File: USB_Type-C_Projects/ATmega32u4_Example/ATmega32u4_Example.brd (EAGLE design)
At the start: 29.1 x 61.5 mm, 8 parts, among them J2 105450-0101, U1 ATMEGA32U4-AU, U2 IP4234CZ6,125

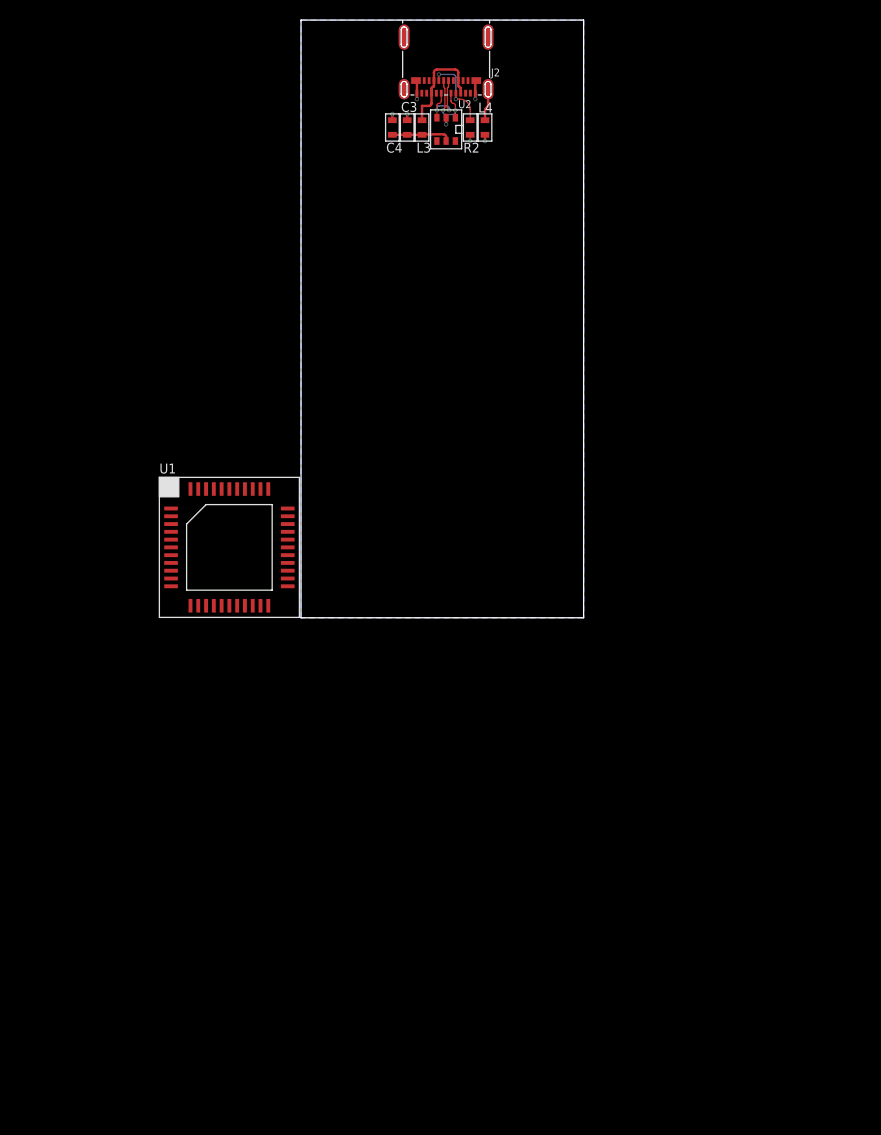
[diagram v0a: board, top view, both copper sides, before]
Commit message: USB connections made.
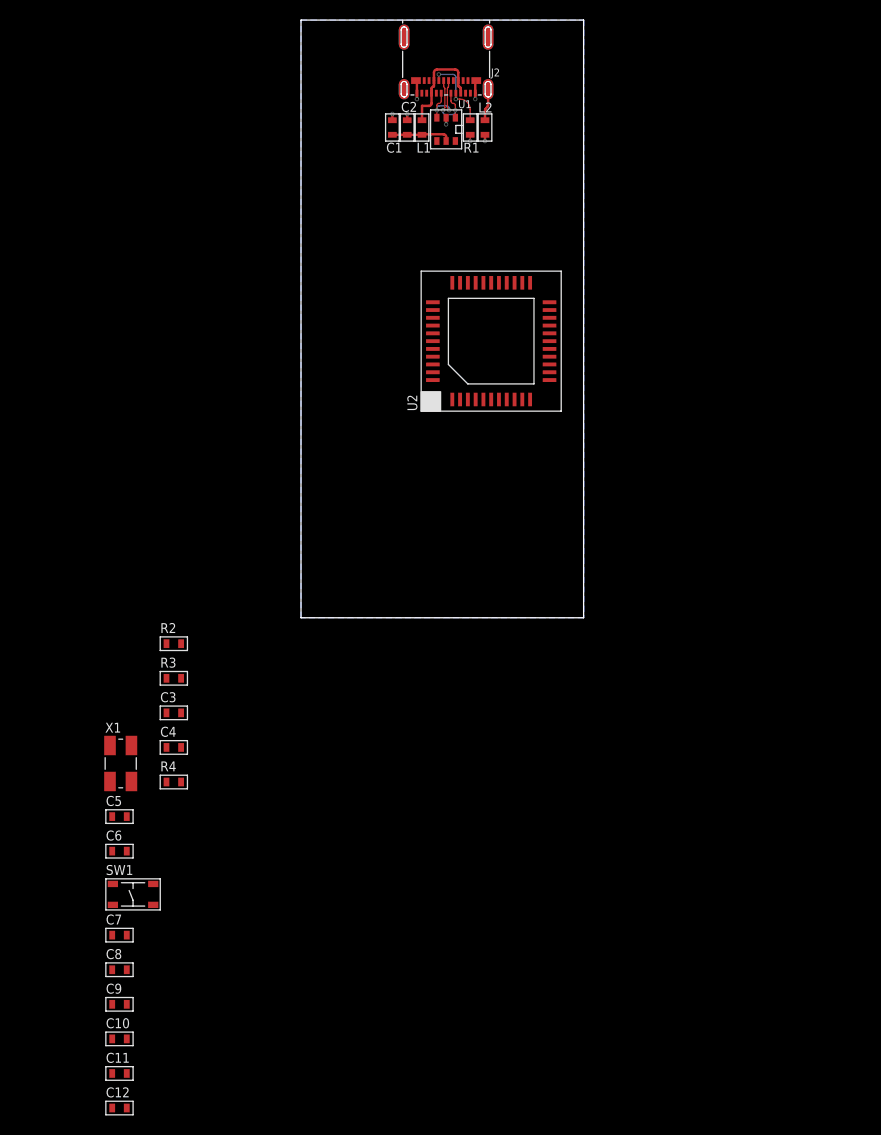
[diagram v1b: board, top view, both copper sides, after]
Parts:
- added C1: 1uF, MF_Passives:C0603
- added C10, C11, C12, C2, C7, C8, C9: 0.1uF, MF_Passives:C0603
- added C5, C6: 22pF, MF_Passives:C0603
- added R1: 5.1K, MF_Passives:R0603
- added R3: 22, MF_Passives:R0603
- added R4: 10K, MF_Passives:R0603
- added SW1: MF-SW-TACT-4.2MM, MF_Switches:TACT4.2MM
- added X1: ABM3B-16.000MHZ-D-1-X-T, MF_Frequency_Control:5MMX3.2MM
- C3: value 0.1uF -> 1uF
- C4: value 1uF -> 0.1uF
- R2: value 5.1K -> 22
- U1: value ATMEGA32U4-AU -> IP4234CZ6,125; device MF_IC_Digital:TQFP44 -> PP_Passives:IP4234CZ6_SOT-457-6
- U2: value IP4234CZ6,125 -> ATMEGA32U4-AU; device PP_Passives:IP4234CZ6_SOT-457-6 -> MF_IC_Digital:TQFP44
- moved C4 67.6 mm to (-13.1, -13.3), turned to 0 degrees
- moved C3 64.8 mm to (-13.1, -9.78), turned to 0 degrees
- moved R2 61.2 mm to (-13.1, -2.67), turned to 0 degrees
- moved U1 48.4 mm to (14.9, 50.2), turned to 270 degrees
- moved U2 22.3 mm to (19.6, 28.4), turned to 90 degrees
- renumbered L3 to L1, L4 to L2
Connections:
- removed net AREF: U1.P$42
- removed net AVCC: U1.P$24, U1.P$44
- removed net UCAP: U1.P$6
- removed net UGND: U1.P$5
- removed net UVCC: U1.P$2
- removed net VBUS: U1.P$7
- removed net VCC: U1.P$14, U1.P$34
- new net N$1: R2.P$2, U2.P$3
- new net N$2: R3.P$2, U2.P$4
- new net N$3: C3.P$2, U2.P$6
- new net N$4: C4.P$2, U2.P$42
- new net RESET: R4.P$2, SW1.P$1, SW1.P$2, U2.P$13
- new net XTAL1: C5.P$1, U2.P$17, X1.P$1
- new net XTAL2: C6.P$1, U2.P$16, X1.P$3
- net CC1/1: now also R1.P$1; no longer R2.P$1
- net D+: now also U1.1; no longer U2.1
- net D-: now also U1.3; no longer U2.3
- net DM: now also R2.P$1, U1.4; no longer U2.4
- net DP: now also R3.P$1, U1.6; no longer U2.6
- net GND: now also C1.P$2, C10.P$2, C11.P$2, C12.P$2, C2.P$2, C3.P$1, C4.P$1, C5.P$2, C6.P$2, C7.P$2, C8.P$2, C9.P$2, R1.P$2, SW1.P$3, SW1.P$4, U1.2, U2.P$15, U2.P$23, U2.P$35, U2.P$43, U2.P$5, X1.P$2, X1.P$4; no longer C3.P$2, C4.P$2, R2.P$2, U1.P$15, U1.P$23, U1.P$35, U1.P$43, U2.2
- net USB_VBUS: now also C1.P$1, C10.P$1, C11.P$1, C12.P$1, C2.P$1, C7.P$1, C8.P$1, C9.P$1, R4.P$1, U1.5, U2.P$14, U2.P$2, U2.P$24, U2.P$34, U2.P$44, U2.P$7; no longer C3.P$1, C4.P$1, U2.5

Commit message: Schematic complete. Parts placed.
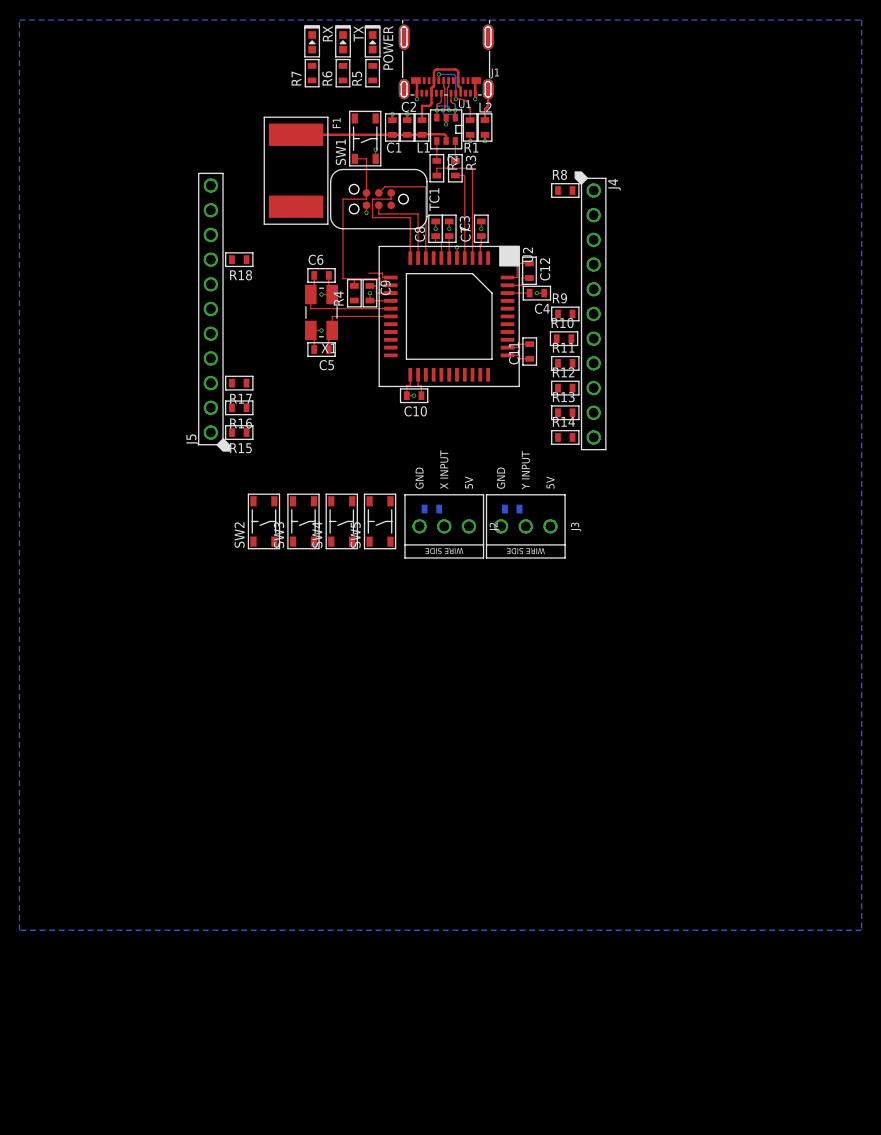
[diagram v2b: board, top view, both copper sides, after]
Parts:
- added C13, C14: 0.1uF, MF_Passives:C0603
- added F1: 0ZCF0050FF2C, PP_Passives:2920
- added J1: 105450-0101, PP_Connectors:105450-0101
- added J3: 282834-3, PP_Connectors:282834-3
- added J4, J5: MF-CON-2.54mm-01x11, MF_Connectors:PTH_2.54MM_01X11
- added POWER, RX, TX: MF-LED-0603-RED, MF_LEDs:LED0603
- added R10, R11, R12, R13, R14, R15, R16, R17, R18, R8, R9: 10K, MF_Passives:R0603
- added R5, R6, R7: 330, MF_Passives:R0603
- added SW2, SW3, SW4, SW5: MF-SW-TACT-4.2MM, MF_Switches:TACT4.2MM
- added TC1: TC2030-IDC-NL, MF_Connectors:TC2030-IDC-NL
- J2: value 105450-0101 -> 282834-3; device PP_Connectors:105450-0101 -> PP_Connectors:282834-3
- moved C12 95.9 mm to (23.5, 35.7), turned to 270 degrees
- moved C11 85.4 mm to (23.5, 27.4), turned to 90 degrees
- moved C8 82.8 mm to (13.8, 40.0), turned to 90 degrees
- moved C7 81.6 mm to (18.5, 40.0), turned to 90 degrees
- moved SW1 81.3 mm to (6.60, 49.3), turned to 90 degrees
- moved C9 77.5 mm to (7.09, 33.4), turned to 270 degrees
- moved C10 72.8 mm to (11.6, 22.8), turned to 180 degrees
- moved C6 62.7 mm to (2.11, 35.2)
- moved R3 59.9 mm to (15.9, 46.2), turned to 270 degrees
- moved C4 59.8 mm to (24.3, 33.4), turned to 180 degrees
- moved C3 57.3 mm to (15.2, 40.0), turned to 270 degrees
- moved R2 55.9 mm to (14.0, 46.2), turned to 270 degrees
- moved R4 53.6 mm to (5.49, 33.4), turned to 90 degrees
- moved C5 52.3 mm to (2.11, 27.6), turned to 180 degrees
- moved X1 50.8 mm to (2.11, 31.4), turned to 180 degrees
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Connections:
- new net 5V: C10.P$1, C11.P$1, C12.P$1, C7.P$1, C8.P$1, C9.P$1, F1.2, J2.P$1, J3.P$1, J5.P$9, R10.P$1, R11.P$1, R12.P$1, R13.P$1, R14.P$1, R15.P$1, R16.P$1, R17.P$1, R18.P$1, R4.P$1, R5.P$1, R8.P$1, R9.P$1, TC1.P$2, U2.P$14, U2.P$2, U2.P$24, U2.P$34, U2.P$44, U2.P$7
- new net A0: C13.P$1, J2.P$2, U2.P$36
- new net A1: C14.P$1, J3.P$2, U2.P$37
- new net A2: J4.P$5, U2.P$38
- new net A3: J4.P$4, U2.P$39
- new net A4: J4.P$3, U2.P$40
- new net A5: J4.P$2, U2.P$41
- new net D0/RX: J5.P$5, U2.P$20
- new net D1/TX: J5.P$4, U2.P$21
- new net D2/SDA: J5.P$6, U2.P$19
- new net D3/SCL: J5.P$7, U2.P$18
- new net D4: J5.P$3, R17.P$2, SW2.P$1, SW2.P$2, U2.P$25
- new net D5*: J4.P$8, R11.P$2, SW3.P$1, SW3.P$2, U2.P$31
- new net D6*: J5.P$1, R15.P$2, SW4.P$1, SW4.P$2, U2.P$27
- new net D7: J4.P$1, R8.P$2, SW5.P$1, SW5.P$2, U2.P$1
- new net HWB: J4.P$6, R9.P$2, U2.P$33
- new net IO10*: J4.P$9, R12.P$2, U2.P$30
- new net IO11*: J5.P$8, R18.P$2, U2.P$12
- new net IO12: J5.P$2, R16.P$2, U2.P$26
- new net IO13*: J4.P$7, R10.P$2, U2.P$32
- new net IO8: J4.P$11, R14.P$2, U2.P$28
- new net IO9*: J4.P$10, R13.P$2, U2.P$29
- new net MISO: TC1.P$1, U2.P$11
- new net MOSI: TC1.P$4, U2.P$10
- new net N$5: POWER.ANODE, R5.P$2
- new net N$6: R6.P$2, TX.ANODE
- new net N$7: R7.P$2, RX.ANODE
- new net RXLED: R7.P$1, U2.P$8
- new net SCK: TC1.P$3, U2.P$9
- new net TXLED: R6.P$1, U2.P$22
- net CC1/1: now also J1.A5, J1.B5; no longer J2.A5, J2.B5
- net D+: now also J1.A6, J1.B6; no longer J2.A6, J2.B6
- net D-: now also J1.A7, J1.B7; no longer J2.A7, J2.B7
- net GND: now also C13.P$2, C14.P$2, J1.A1, J1.A12, J1.B1, J1.B12, J2.P$3, J3.P$3, J5.P$10, POWER.CATHODE, RX.CATHODE, SW2.P$3, SW2.P$4, SW3.P$3, SW3.P$4, SW4.P$3, SW4.P$4, SW5.P$3, SW5.P$4, TC1.P$6, TX.CATHODE; no longer J2.A1, J2.A12, J2.B1, J2.B12, SW1.P$4
- net RESET: now also TC1.P$5; no longer SW1.P$2
- net SHEILD1: now also J1.S_T1, J1.S_T2, J1.S_T3, J1.S_T4; no longer J2.S_T1, J2.S_T2, J2.S_T3, J2.S_T4
- net USB_VBUS: now also F1.1; no longer C10.P$1, C11.P$1, C12.P$1, C7.P$1, C8.P$1, C9.P$1, R4.P$1, U2.P$14, U2.P$2, U2.P$24, U2.P$34, U2.P$44, U2.P$7
- net USB_VBUS_PORT: now also J1.A4, J1.A9, J1.B4, J1.B9; no longer J2.A4, J2.A9, J2.B4, J2.B9
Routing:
- net GND: track 7.29 -> 31.7 mm, vias 7 -> 18
- net RESET: track 0.00 -> 22.3 mm
- net 5V: track 0.00 -> 17.0 mm
- net N$1: track 0.00 -> 13.7 mm
- net MISO: track 0.00 -> 12.5 mm
- net SCK: track 0.00 -> 12.4 mm
- net XTAL2: track 0.00 -> 12.0 mm
- net USB_VBUS: track 6.12 -> 16.0 mm
- net XTAL1: track 0.00 -> 9.79 mm
- net MOSI: track 0.00 -> 9.47 mm
- net N$2: track 0.00 -> 9.46 mm
- net IO11*: track 0.00 -> 2.70 mm
- net N$4: track 0.00 -> 2.27 mm
- net N$3: track 0.00 -> 2.27 mm
- net DP: track 0.00 -> 2.05 mm
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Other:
- board size 29.1 x 61.5 mm -> 9.2 x 7.2 mm

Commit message: Routing complete
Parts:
- removed SW2, SW3, SW4, SW5: MF-SW-TACT-4.2MM, MF_Switches:TACT4.2MM
- added C15: 0.1uF, MF_Passives:C0603
- moved J2 22.3 mm to (-7.24, 13.5), turned to 90 degrees
- moved C13 19.0 mm to (-5.21, 14.9), turned to 90 degrees
- moved F1 12.2 mm to (3.68, 57.4), turned to 180 degrees
- moved POWER 9.45 mm to (2.54, 51.1)
- moved R5 9.45 mm to (2.54, 47.9)
- moved R6 9.45 mm to (-0.51, 47.9)
- moved R7 9.45 mm to (-3.68, 47.9)
- moved RX 9.45 mm to (-3.68, 51.1)
- moved TX 9.45 mm to (-0.51, 51.1)
- moved J3 6.10 mm to (28.1, 13.0), turned to 270 degrees
- moved C14 4.33 mm to (26.0, 11.6), turned to 270 degrees
- moved C9 0.38 mm to (6.71, 33.4)
- moved R4 0.38 mm to (5.11, 33.4)
- moved R10 0.13 mm to (27.2, 28.7), flipped to the bottom, turned to 180 degrees
- moved C3 0.13 mm to (15.4, 40.0)
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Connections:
- net 5V: now also R6.P$1, R7.P$1
- net D4: no longer SW2.P$1, SW2.P$2
- net D5*: no longer SW3.P$1, SW3.P$2
- net D6*: no longer SW4.P$1, SW4.P$2
- net D7: no longer SW5.P$1, SW5.P$2
- net GND: now also C15.P$2, J5.P$11; no longer RX.CATHODE, SW2.P$3, SW2.P$4, SW3.P$3, SW3.P$4, SW4.P$3, SW4.P$4, SW5.P$3, SW5.P$4, TX.CATHODE
- net RESET: now also C15.P$1
- net RXLED: now also RX.CATHODE; no longer R7.P$1
- net TXLED: now also TX.CATHODE; no longer R6.P$1
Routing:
- net 5V: track 17.0 -> 267.3 mm, vias 0 -> 8
- net A0: track 0.00 -> 68.4 mm
- net TXLED: track 0.00 -> 46.7 mm, vias 0 -> 2
- net A1: track 0.00 -> 34.6 mm
- net D4: track 0.00 -> 31.1 mm
- net D6*: track 0.00 -> 31.0 mm
- net IO12: track 0.00 -> 30.9 mm
- net RXLED: track 0.00 -> 29.8 mm
- net D3/SCL: track 0.00 -> 23.2 mm
- net D2/SDA: track 0.00 -> 22.3 mm
- net D0/RX: track 0.00 -> 21.3 mm
- net IO8: track 0.00 -> 20.4 mm
- net D1/TX: track 0.00 -> 20.3 mm
- net IO13*: track 0.00 -> 19.5 mm
- net HWB: track 0.00 -> 19.3 mm
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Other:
- board size 9.2 x 7.2 mm -> 42.5 x 52.8 mm

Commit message: PCB complete. First rev ordered.
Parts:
- added FRAME1: MF_FRAMEDEFAULT, MF_Aesthetics:MF_FRAME_DEFAULT
- added H1, H2, H3, H4: MOUNT_HOLE150MIL, PP_Connectors:MOUNT_HOLE_150MIL
- moved RX 14.0 mm to (8.51, 44.2)
- moved R7 13.9 mm to (8.51, 41.1)
- moved TX 13.7 mm to (11.3, 44.2)
- moved R6 13.6 mm to (11.3, 41.1)
- moved POWER 13.4 mm to (14.1, 44.2)
- moved R5 13.4 mm to (14.1, 41.1)
- moved F1 13.0 mm to (15.0, 51.1)
- moved SW1 12.9 mm to (17.7, 42.7)
- moved C1 12.7 mm to (20.2, 43.8)
- moved J1 12.7 mm to (25.7, 47.8)
- moved L1 12.7 mm to (23.2, 43.8)
- moved L2 12.7 mm to (29.7, 43.8)
- moved R2 12.7 mm to (24.8, 39.6)
- moved R3 12.7 mm to (26.7, 39.6)
- moved U1 12.7 mm to (25.7, 43.6)
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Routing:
- net 5V: track 267.3 -> 246.2 mm, vias 8 -> 7
- net HWB: track 19.3 -> 26.6 mm
- net A3: track 11.9 -> 18.9 mm
- net A5: track 15.6 -> 22.6 mm
- net A4: track 13.8 -> 20.7 mm
- net A2: track 10.3 -> 17.0 mm
- net A1: track 34.6 -> 40.8 mm
- net IO13*: track 19.5 -> 25.7 mm
- net D5*: track 18.5 -> 24.6 mm
- net D3/SCL: track 23.2 -> 28.5 mm
- net A0: track 68.4 -> 73.6 mm
- net IO10*: track 18.8 -> 23.9 mm
- net D7: track 16.5 -> 21.4 mm
- net D2/SDA: track 22.3 -> 26.5 mm
- net IO9*: track 18.9 -> 22.9 mm
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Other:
- board size 42.5 x 52.8 mm -> 40.3 x 54.9 mm

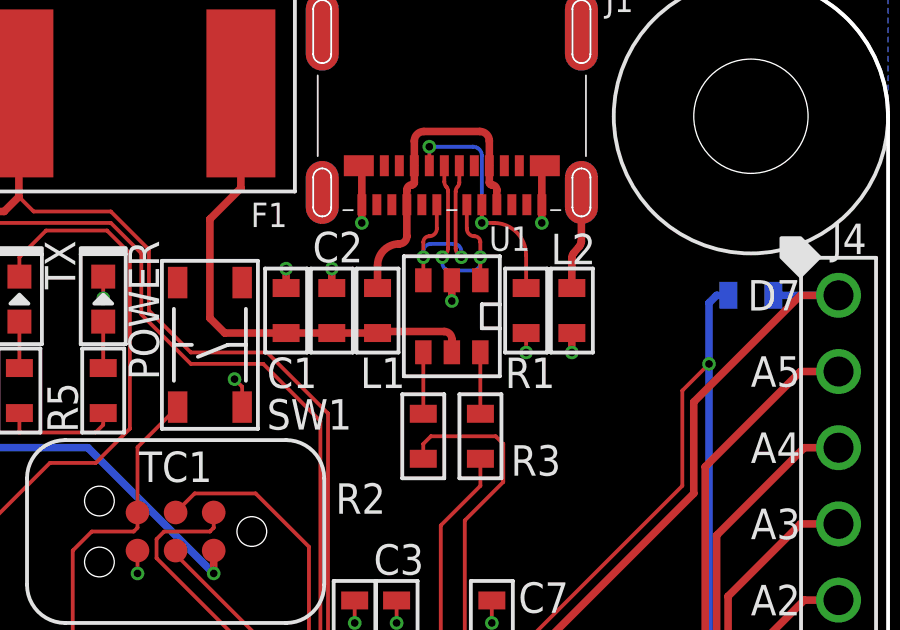
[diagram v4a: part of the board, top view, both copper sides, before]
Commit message: Fixed IP4234CZ6 ESD protection
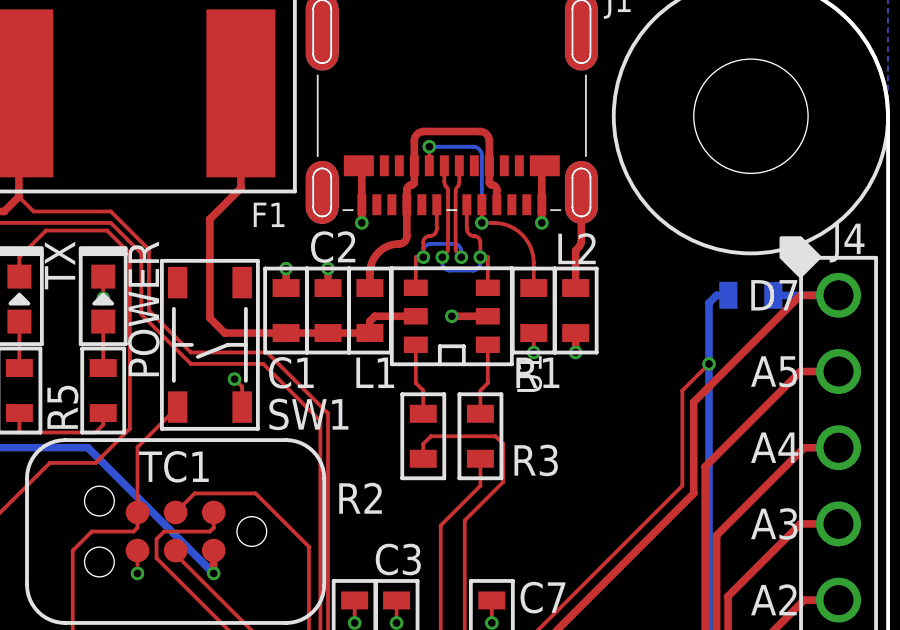
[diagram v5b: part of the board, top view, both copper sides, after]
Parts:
- moved L1 0.25 mm to (23.0, 43.8)
- moved R1 0.25 mm to (28.4, 43.8)
- moved C2 0.13 mm to (21.6, 43.8)
- moved L2 0.13 mm to (29.8, 43.8)
- turned U1 to 180 degrees
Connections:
- net D+: now also U1.3; no longer U1.1
- net D-: now also U1.4; no longer U1.3
- net DM: now also U1.6; no longer U1.4
- net DP: now also U1.1; no longer U1.6
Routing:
- net USB_VBUS: track 16.8 -> 15.5 mm
- net GND: track 34.3 -> 34.8 mm
- net D-: track 7.70 -> 8.20 mm
- net D+: track 7.70 -> 8.20 mm
